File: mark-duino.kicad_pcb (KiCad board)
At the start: 4 copper layers, 111.8 x 61 mm, 57 parts, among them IC1 ATmega328P, J1 Conn_FTDI, J2 IC1_Analog, J3 IC1_SPI, J4 IC1_Digital, J5 12VDC_IN, J6 IC1_I2C, J7 Conn_12V, J8 MCP_Analog, J9 Conn_5V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

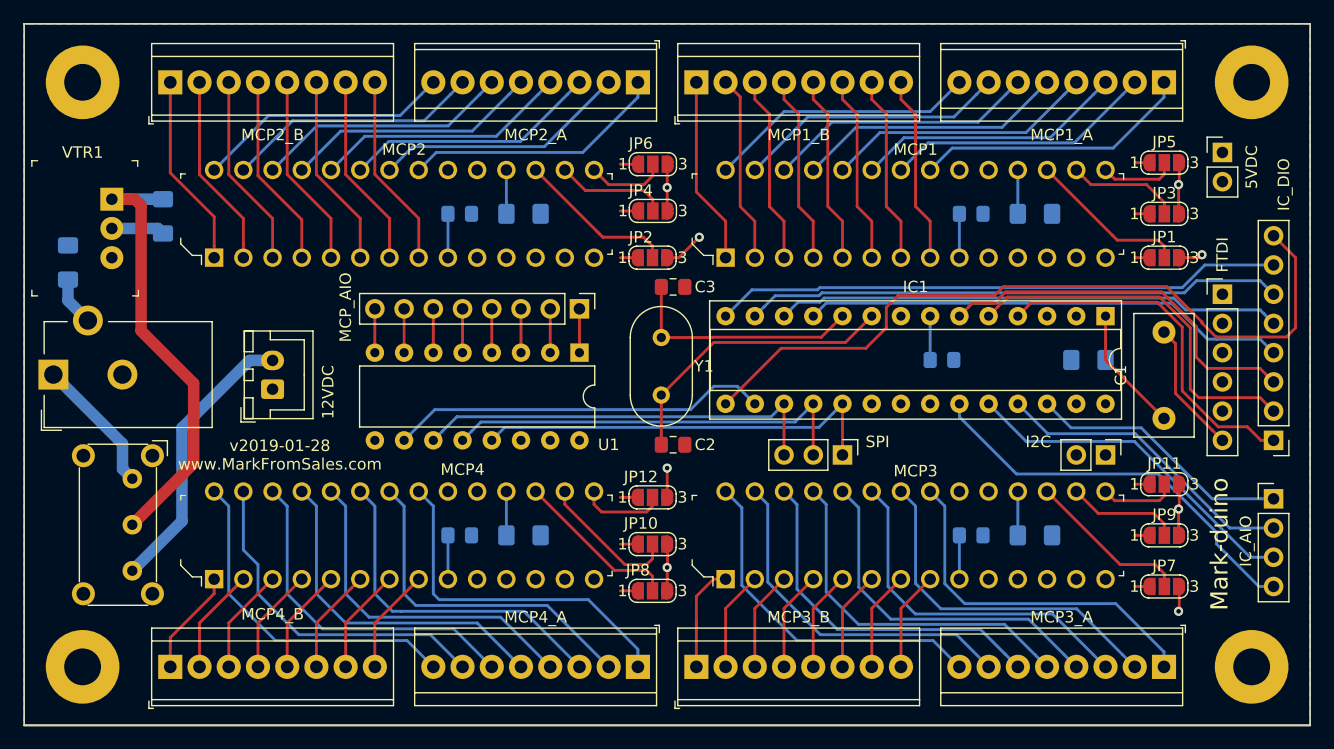
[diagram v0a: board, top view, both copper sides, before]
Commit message: Rounded corners
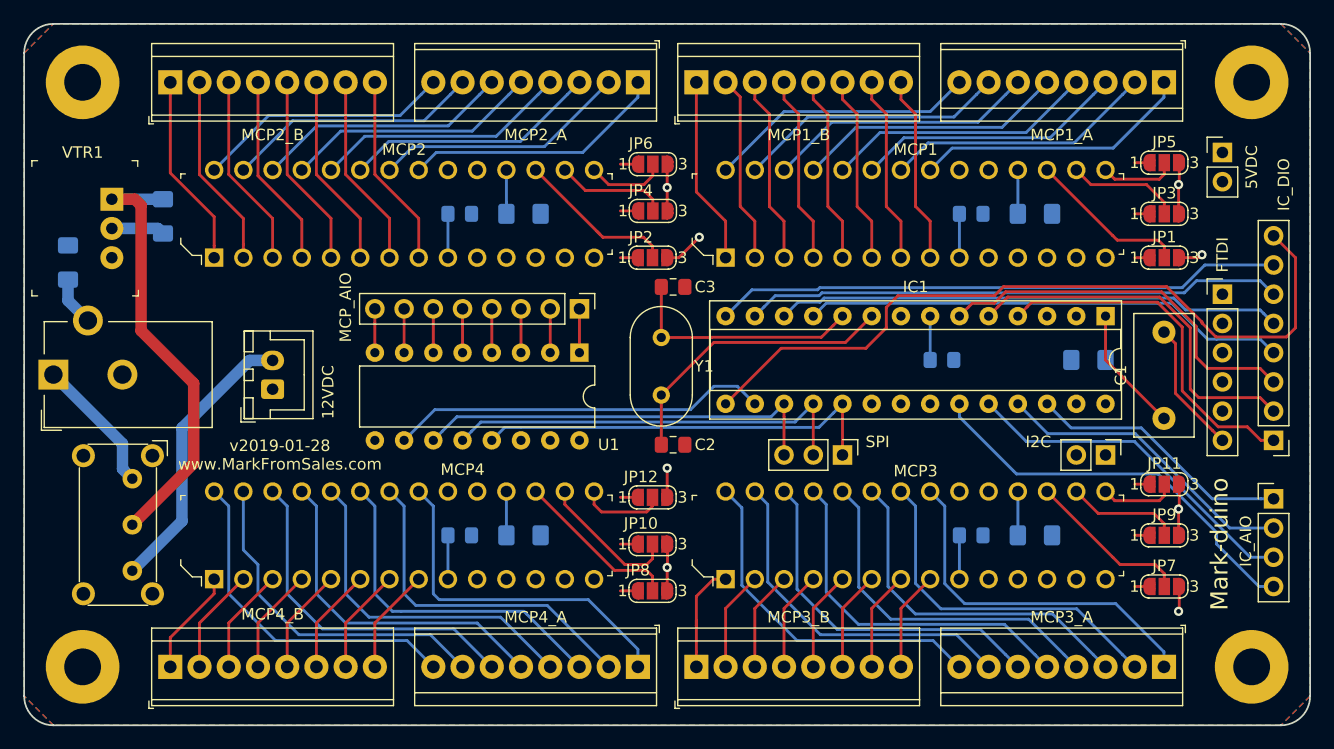
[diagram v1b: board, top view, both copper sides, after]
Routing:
- added copper zone on In2.Cu, net GND
- removed copper zone on In2.Cu, net +5V
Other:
- outline, holes or cut-outs redrawn
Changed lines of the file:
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@@
   (general
     (thickness 1.6)
-    (drawings 23)
+    (drawings 27)
     (tracks 563)
     (zones 0)
@@
     )
   )
+  (gr_arc (start 149.86 27.94) (end 149.86 25.4) (angle -90) (layer Edge.Cuts) (width 0.15))
+  (gr_arc (start 149.86 83.82) (end 147.32 83.82) (angle -90) (layer Edge.Cuts) (width 0.15))
+  (gr_arc (start 256.54 83.82) (end 256.54 86.36) (angle -90) (layer Edge.Cuts) (width 0.15))
+  (gr_line (start 149.86 86.36) (end 256.54 86.36) (layer Edge.Cuts) (width 0.15))
+  (gr_arc (start 256.54 27.94) (end 259.08 27.94) (angle -90) (layer Edge.Cuts) (width 0.15))
   (gr_text "v2019-01-28\nwww.MarkFromSales.com" (at 169.545 62.865) (layer F.SilkS)
     (effects (font (size 1 1) (thickness 0.15)))
@@
     (effects (font (size 1.5 1.5) (thickness 0.3)))
   )
-  (gr_line (start 259.08 86.36) (end 147.32 86.36) (layer Edge.Cuts) (width 0.2))
-  (gr_line (start 259.08 25.4) (end 259.08 86.36) (layer Edge.Cuts) (width 0.15))
-  (gr_line (start 147.32 86.36) (end 147.32 25.4) (layer Edge.Cuts) (width 0.15))
-  (gr_line (start 147.32 25.4) (end 259.08 25.4) (layer Edge.Cuts) (width 0.15))
+  (gr_line (start 259.08 27.94) (end 259.08 83.82) (layer Edge.Cuts) (width 0.15))
+  (gr_line (start 147.32 83.82) (end 147.32 27.94) (layer Edge.Cuts) (width 0.15))
+  (gr_line (start 149.86 25.4) (end 256.54 25.4) (layer Edge.Cuts) (width 0.15))
   (segment (start 241.3 54.61) (end 241.3 50.8) (width 0.25) (layer B.Cu) (net 1))
   (segment (start 241.3 54.61) (end 246.38 59.69) (width 0.25) (layer F.Cu) (net 1))
@@
     (polygon
       (pts
-        (xy 147.32 25.4) (xy 147.32 86.36) (xy 259.08 86.36) (xy 259.08 25.4)
+        (xy 149.86 25.4) (xy 256.54 25.4) (xy 259.08 27.94) (xy 259.08 83.82) (xy 256.54 86.36)
+        (xy 149.86 86.36) (xy 147.32 83.82) (xy 147.32 27.94)
       )
     )
   )
-  (zone (net 7) (net_name +5V) (layer B.Cu) (hatch edge 0.508)
+  (zone (net 3) (net_name GND) (layer In1.Cu) (hatch edge 0.508)
     (connect_pads (clearance 0.508))
     (min_thickness 0.254)
@@
     (polygon
       (pts
-        (xy 147.32 25.4) (xy 147.32 86.36) (xy 259.08 86.36) (xy 259.08 25.4)
+        (xy 149.86 25.4) (xy 256.54 25.4) (xy 259.08 27.94) (xy 259.08 83.82) (xy 256.54 86.36)
+        (xy 149.86 86.36) (xy 147.32 83.82) (xy 147.32 27.94)
       )
     )
   )
-  (zone (net 7) (net_name +5V) (layer In2.Cu) (hatch edge 0.508)
+  (zone (net 3) (net_name GND) (layer In2.Cu) (hatch edge 0.508)
     (connect_pads (clearance 0.508))
     (min_thickness 0.254)
@@
     (polygon
       (pts
-        (xy 147.32 25.4) (xy 259.08 25.4) (xy 259.08 86.36) (xy 147.32 86.36)
+        (xy 149.86 25.4) (xy 256.54 25.4) (xy 259.08 27.94) (xy 259.08 83.82) (xy 256.54 86.36)
+        (xy 149.86 86.36) (xy 147.32 83.82) (xy 147.32 27.94)
       )
     )
   )
-  (zone (net 3) (net_name GND) (layer In1.Cu) (hatch edge 0.508)
+  (zone (net 7) (net_name +5V) (layer B.Cu) (hatch edge 0.508)
     (connect_pads (clearance 0.508))
     (min_thickness 0.254)
@@
     (polygon
       (pts
-        (xy 147.32 25.4) (xy 147.32 86.36) (xy 259.08 86.36) (xy 259.08 25.4)
+        (xy 149.86 25.4) (xy 256.54 25.4) (xy 259.08 27.94) (xy 259.08 83.82) (xy 256.54 86.36)
+        (xy 149.86 86.36) (xy 147.32 83.82) (xy 147.32 27.94)
       )
     )
